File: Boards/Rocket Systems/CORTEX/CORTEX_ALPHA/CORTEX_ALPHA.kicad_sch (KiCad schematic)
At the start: 1 part, among them U1 NUCLEO-F302R8

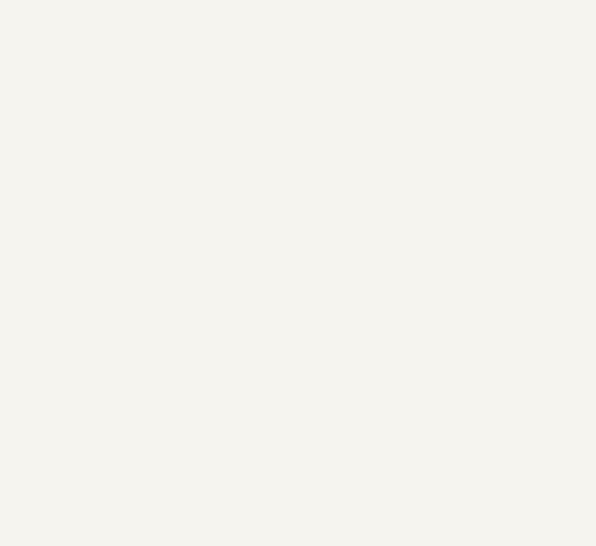
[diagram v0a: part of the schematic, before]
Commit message: added radio module
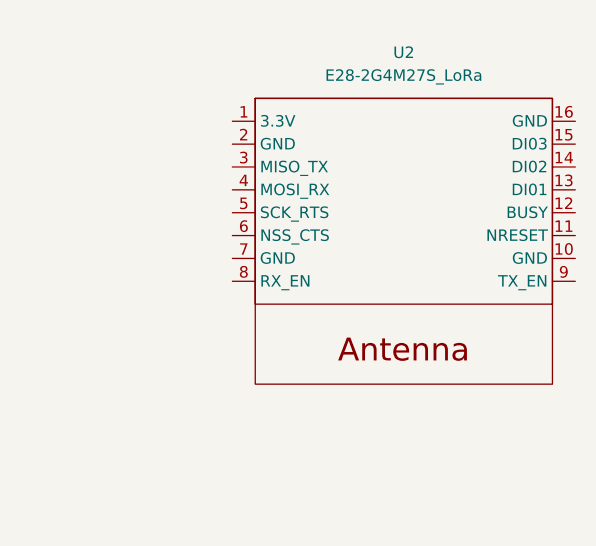
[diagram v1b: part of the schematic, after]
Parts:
- added U2: E28-2G4M27S_LoRa, CORTEX:E28-2G4M27S, symbol MyNewSymbolLibrary:E28-2G4M27S_LoRa
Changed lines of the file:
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@@
+	)
+	(symbol
+		(lib_id "MyNewSymbolLibrary:E28-2G4M27S_LoRa")
+		(at 182.88 74.93 0)
+		(unit 1)
+		(exclude_from_sim no)
+		(in_bom yes)
+		(on_board yes)
+		(dnp no)
+		(fields_autoplaced yes)
+		(property "Reference" "U2"
+			(at 182.88 63.5 0)
+			(effects
+				(font
+					(size 1.27 1.27)
+				)
+			)
+		)
+		(property "Value" "E28-2G4M27S_LoRa"
+			(at 182.88 66.04 0)
+			(effects
+				(font
+					(size 1.27 1.27)
+				)
+			)
+		)
+		(property "Footprint" "CORTEX:E28-2G4M27S"
+			(at 185.42 81.28 90)
+			(effects
+				(font
+					(size 1.27 1.27)
+				)
+				(hide yes)
+			)
+		)
+		(property "Datasheet" ""
+			(at 185.42 81.28 90)
+			(effects
+				(font
+					(size 1.27 1.27)
+				)
+				(hide yes)
+			)
+		)
+		(property "Description" ""
+			(at 182.88 74.93 0)
+			(effects
+				(font
+					(size 1.27 1.27)
+				)
+			)
+		)
+		(pin "1"
+		)
+		(pin "10"
+		)
+		(pin "11"
+		)
+		(pin "12"
+		)
+		(pin "13"
+		)
+		(pin "14"
+		)
+		(pin "15"
+		)
+		(pin "16"
+		)
+		(pin "2"
+		)
+		(pin "3"
+		)
+		(pin "4"
+		)
+		(pin "5"
+		)
+		(pin "6"
+		)
+		(pin "7"
+		)
+		(pin "8"
+		)
+		(pin "9"
+		)
+		(instances
+			(project "CORTEX_ALPHA"
+				(path "/b3433ded-bc33-4d30-8ca0-59a8e98dfeda"
+					(reference "U2")
+					(unit 1)
+				)
+			)
+		)
 	)
 	(symbol

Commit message: edge cuts
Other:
- moved on the sheet: U2
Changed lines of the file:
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@@
 	(symbol
 		(lib_id "MyNewSymbolLibrary:E28-2G4M27S_LoRa")
-		(at 182.88 74.93 0)
+		(at 208.28 78.74 0)
 		(unit 1)
 		(exclude_from_sim no)
@@
 		(fields_autoplaced yes)
 		(property "Reference" "U2"
-			(at 182.88 63.5 0)
+			(at 208.28 67.31 0)
 			(effects
 				(font
@@
 		)
 		(property "Value" "E28-2G4M27S_LoRa"
-			(at 182.88 66.04 0)
+			(at 208.28 69.85 0)
 			(effects
 				(font
@@
 		)
 		(property "Footprint" "CORTEX:E28-2G4M27S"
-			(at 185.42 81.28 90)
+			(at 210.82 85.09 90)
 			(effects
 				(font
@@
 		)
 		(property "Datasheet" ""
-			(at 185.42 81.28 90)
+			(at 210.82 85.09 90)
 			(effects
 				(font
@@
 		)
 		(property "Description" ""
-			(at 182.88 74.93 0)
+			(at 208.28 78.74 0)
 			(effects
 				(font

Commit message: Main components placed
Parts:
- added CanBus_Module1: ~, CORTEX:Canbus, symbol CanBus:MCP2551_Module
- added U3: MAX485_MODULE_5V_LOGIC_TLL_TO_RS-485_CONVERTER, MAX485_MODULE_5V_LOGIC_TLL_TO_RS-485_CONVERTER:MODULE_MAX485_MODULE_5V_LOGIC_TLL_TO_RS-485_CONVERTER, symbol MAX485_MODULE_5V_LOGIC_TLL_TO_RS-485_CONVERTER:MAX485_MODULE_5V_LOGIC_TLL_TO_RS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
- added U4: ~, LIFT:MicroSD Reader, symbol LIFT:MicroSD_Reader

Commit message: progress
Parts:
- removed U1: NUCLEO-F302R8, MyLibrary:MODULE_NUCLEO-F302R8, symbol NUCLEO-F302R8:NUCLEO-F302R8
- added U5: ~, CORTEX:DCDC_Module, symbol Mini Dc-Dc:MiniDCDCBoost

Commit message: Cortex Update
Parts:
- added C1, C4: 10uF, Capacitor_SMD:C_0603_1608Metric_Pad1.08x0.95mm_HandSolder, symbol Device:C
- added C2, C3: 47uF, Capacitor_SMD:C_0603_1608Metric_Pad1.08x0.95mm_HandSolder, symbol Device:C
- added C5: 100uF, Capacitor_SMD:C_0603_1608Metric_Pad1.08x0.95mm_HandSolder, symbol Device:C
- added C6: 0.1uF, Capacitor_SMD:C_0603_1608Metric_Pad1.08x0.95mm_HandSolder, symbol Device:C
- added J2: Screw_Terminal_01x02, TerminalBlock:TerminalBlock_Xinya_XY308-2.54-2P_1x02_P2.54mm_Horizontal, symbol Connector:Screw_Terminal_01x02
- added J3: 1200700164, CONN_1200700164_MOL, symbol CONN_1200700164_MOL:1200700164
- added R1: 1K, Resistor_SMD:R_0603_1608Metric_Pad0.98x0.95mm_HandSolder, symbol Device:R
- added R2: 10K, Resistor_SMD:R_0603_1608Metric_Pad0.98x0.95mm_HandSolder, symbol Device:R
- added U1: YAAJ_BluePill, STM32 Blue Pill:YAAJ_BluePill_1, symbol YAAJ_BluePill:YAAJ_BluePill
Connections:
- net +3.3V: now reaches U2.1 (3.3V)
- net +3.3V: now also U4.6 (3.3V), C5.1, C6.1, U1.20 (3V3), U1.38 (3V3)
- net GND: now reaches U2.10 (GND)
- net GND: now also CanBus_Module1.5 (GND), U2.16 (GND), U2.2 (GND), U2.7 (GND), U3.1 (GND), U4.1 (GND), U5.2 (IN-), U5.4 (OUT-), C1.2, C2.2, C3.2, C4.2, C5.2, C6.2, J3.2, R1.2, R2.2, U1.19 (GND), U1.39 (GND), U1.40 (GND)
- net ANT_NRESET: now reaches U2.11 (NRESET)
- net ANT_NRESET: now also U1.35 (PB10)
- net ANT_BUSY: now reaches U2.12 (BUSY)
- net ANT_BUSY: now also U1.34 (PB1)
- net ANT_DIO1: now reaches U2.13 (DI01)
- net ANT_DIO1: now also R2.1, U1.33 (PB0)
- net ANT_MISO: now reaches U2.3 (MISO_TX)
- net ANT_MISO: now also U1.12 (PB4)
- net ANT_MOSI: now reaches U2.4 (MOSI_RX)
- net ANT_MOSI: now also U1.13 (PB5)
- net ANT_SCK: now reaches U2.5 (SCK_RTS)
- net ANT_SCK: now also U1.11 (PB3)
- net ANT_NSS: now reaches U2.6 (NSS_CTS)
- net ANT_NSS: now also U1.10 (PA15)
- net ANT_RX_EN: now reaches U2.8 (RX_EN)
- net ANT_RX_EN: now also U1.26 (PA1)
- net ANT_TX_EN: now reaches U2.9 (TX_EN)
- net ANT_TX_EN: now also U1.25 (PA0)
- net RS_A: now reaches U3.2 (A)
- net RS_A: now also J3.3
- net RS_B: now reaches U3.3 (B)
- net RS_B: now also J3.4
- net +5V: now reaches U3.4 (VCC)
- net +5V: now also CanBus_Module1.6 (VCC), U5.3 (OUT+), C1.1, C2.1, U1.18 (5V)
- net RS_RX: now reaches U3.5 (RO)
- net RS_RX: now also U1.7 (PA10)
- net RS_ENABLE: now reaches U3.6 (RE)
- net RS_ENABLE: now also U3.7 (DE), R1.1, U1.5 (PA8)
- net RS_TX: now reaches U3.8 (DI)
- net RS_TX: now also U1.6 (PA9)
- net at CanBus_Module1.1 (CANL): now also J2.1 (Pin_1)
- net at CanBus_Module1.2 (CANH): now also J2.2 (Pin_2)
- net CAN_RX: now reaches CanBus_Module1.3 (CRX)
- net CAN_RX: now also U1.8 (PA11)
- net CAN_TX: now reaches CanBus_Module1.4 (CTX)
- net CAN_TX: now also U1.9 (PA12)
- net SD_MISO: now reaches U4.2 (MISO)
- net SD_MISO: now also U1.31 (PA6)
- net SD_CLK: now reaches U4.3 (CLK)
- net SD_CLK: now also U1.30 (PA5)
- net SD_MOSI: now reaches U4.4 (MOSI)
- net SD_MOSI: now also U1.32 (PA7)
- net SD_CS: now reaches U4.5 (CS)
- net SD_CS: now also U1.29 (PA4)
- net +12.8V: now reaches U5.1 (IN+)
- net +12.8V: now also C3.1, C4.1, J3.1
- no-connect marks 1 -> 0
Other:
- note added: "ANTENNA"
- note added: "CANBUS MODULE"
- note added: "CONNECTORS"
- note added: "DCDC 12.8V-5V"
- note added: "MICRO SD CARD MODULE"
- note added: "RS MODULE"
- note added: "STM32 BLUE PILL"
- moved on the sheet: CanBus_Module1, U2, U3, U4, U5

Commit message: PCBs acabadas e modulo de radio feito
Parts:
- removed C5: 100uF, Capacitor_SMD:C_0603_1608Metric_Pad1.08x0.95mm_HandSolder, symbol Device:C
- removed C6: 0.1uF, Capacitor_SMD:C_0603_1608Metric_Pad1.08x0.95mm_HandSolder, symbol Device:C
- U2: footprint CORTEX:E28-2G4M27S -> Radio_Module_PST:Radio_Module_PST
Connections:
- net ANT_DIO1: now also U1.27 (PA2); no longer U1.33 (PB0)
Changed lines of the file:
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@@
 	)
 	(junction
-		(at 147.32 38.1)
-		(diameter 0)
-		(color 0 0 0 0)
-	)
-	(junction
 		(at 59.69 88.9)
 		(diameter 0)
@@
 	)
 	(junction
-		(at 134.62 38.1)
-		(diameter 0)
-		(color 0 0 0 0)
-	)
-	(junction
 		(at 149.86 134.62)
 		(diameter 0)
@@
 	)
 	(junction
-		(at 147.32 45.72)
-		(diameter 0)
-		(color 0 0 0 0)
-	)
-	(junction
 		(at 222.25 50.8)
 		(diameter 0)
@@
 		(color 0 0 0 0)
 	)
-	(junction
-		(at 134.62 45.72)
-		(diameter 0)
-		(color 0 0 0 0)
-	)
 	(wire
 		(pts
@@
 	(wire
 		(pts
-			(xy 147.32 38.1) (xy 157.48 38.1)
+			(xy 132.08 38.1) (xy 157.48 38.1)
 		)
 		(stroke
@@
 	(wire
 		(pts
-			(xy 147.32 45.72) (xy 157.48 45.72)
-		)
-		(stroke
-			(width 0)
-			(type default)
-		)
-	)
-	(wire
-		(pts
-			(xy 132.08 38.1) (xy 134.62 38.1)
+			(xy 132.08 45.72) (xy 157.48 45.72)
 		)
 		(stroke
@@
 	(wire
 		(pts
-			(xy 132.08 45.72) (xy 134.62 45.72)
-		)
-		(stroke
-			(width 0)
-			(type default)
-		)
-	)
-	(wire
-		(pts
 			(xy 49.53 142.24) (xy 53.34 142.24)
 		)
@@
 	(wire
 		(pts
-			(xy 134.62 38.1) (xy 147.32 38.1)
-		)
-		(stroke
-			(width 0)
-			(type default)
-		)
-	)
-	(wire
-		(pts
 			(xy 34.29 140.97) (xy 34.29 142.24)
 		)
@@
 		)
 	)
-	(wire
-		(pts
-			(xy 134.62 45.72) (xy 147.32 45.72)
-		)
-		(stroke
-			(width 0)
-			(type default)
-		)
-	)
 	(bus
 		(pts
@@
 	)
 	(label "ANT_DIO1"
-		(at 33.02 91.44 0)
+		(at 82.55 66.04 0)
 		(effects
 			(font
@@
 		)
 	)
-	(label "ANT_DIO1"
-		(at 82.55 50.8 0)
-		(effects
-			(font
-				(size 1.27 1.27)
-				(thickness 0.254)
-				(bold yes)
-			)
-			(justify left bottom)
-		)
-	)
 	(label "RS_ENABLE"
 		(at 41.91 50.8 180)
@@
 	(symbol
 		(lib_id "Device:C")
-		(at 134.62 41.91 0)
-		(unit 1)
-		(exclude_from_sim no)
-		(in_bom yes)
-		(on_board yes)
-		(dnp no)
-		(fields_autoplaced yes)
-		(property "Reference" "C5"
-			(at 138.43 40.6399 0)
-			(effects
-				(font
-					(size 1.27 1.27)
-				)
-				(justify left)
-			)
-		)
-		(property "Value" "100uF"
-			(at 138.43 43.1799 0)
-			(effects
-				(font
-					(size 1.27 1.27)
-				)
-				(justify left)
-			)
-		)
-		(property "Footprint" "Capacitor_SMD:C_0603_1608Metric_Pad1.08x0.95mm_HandSolder"
-			(at 135.5852 45.72 0)
-			(effects
-				(font
-					(size 1.27 1.27)
-				)
-				(hide yes)
-			)
-		)
-		(property "Datasheet" "~"
-			(at 134.62 41.91 0)
-			(effects
-				(font
-					(size 1.27 1.27)
-				)
-				(hide yes)
-			)
-		)
-		(property "Description" "Unpolarized capacitor"
-			(at 134.62 41.91 0)
-			(effects
-				(font
-					(size 1.27 1.27)
-				)
-				(hide yes)
-			)
-		)
-		(pin "2"
-		)
-		(pin "1"
-		)
-		(instances
-			(project ""
-				(path "/b3433ded-bc33-4d30-8ca0-59a8e98dfeda"
-					(reference "C5")
-					(unit 1)
-				)
-			)
-		)
-	)
-	(symbol
-		(lib_id "Device:C")
 		(at 38.1 146.05 0)
 		(mirror y)
@@
 			)
 		)
-		(property "Footprint" "CORTEX:E28-2G4M27S"
+		(property "Footprint" "Radio_Module_PST:Radio_Module_PST"
 			(at 179.07 53.34 90)
 			(effects
@@
 					(unit 1)
 				)
-			)
-		)
-	)
-	(symbol
-		(lib_id "Device:C")
-		(at 147.32 41.91 0)
-		(unit 1)
-		(exclude_from_sim no)
-		(in_bom yes)
-		(on_board yes)
-		(dnp no)
-		(fields_autoplaced yes)
-		(property "Reference" "C6"
-			(at 151.13 40.6399 0)
-			(effects
-				(font
-					(size 1.27 1.27)
-				)
-				(justify left)
-			)
-		)
-		(property "Value" "0.1uF"
-			(at 151.13 43.1799 0)
-			(effects
-				(font
-					(size 1.27 1.27)
-				)
-				(justify left)
-			)
-		)
-		(property "Footprint" "Capacitor_SMD:C_0603_1608Metric_Pad1.08x0.95mm_HandSolder"
-			(at 148.2852 45.72 0)
-			(effects
-				(font
-					(size 1.27 1.27)
-				)
-				(hide yes)
-			)
-		)
-		(property "Datasheet" "~"
-			(at 147.32 41.91 0)
-			(effects
-				(font
-					(size 1.27 1.27)
-				)
-				(hide yes)
-			)
-		)
-		(property "Description" "Unpolarized capacitor"
-			(at 147.32 41.91 0)
-			(effects
-				(font
-					(size 1.27 1.27)
-				)
-				(hide yes)
-			)
-		)
-		(pin "2"
-		)
-		(pin "1"
-		)
-		(instances
-			(project "CORTEX_ALPHA"
-				(path "/b3433ded-bc33-4d30-8ca0-59a8e98dfeda"
-					(reference "C6")
-					(unit 1)
-				)
